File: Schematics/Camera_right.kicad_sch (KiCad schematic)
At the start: 8 parts, among them J4 Runcam Split 4 v2, U3 TPS22917DBVR

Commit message: assigned footprints ready for pcb design
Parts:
- C24, C25, C26, C27, J4: footprint (none) -> Capacitor_SMD:C_0805_2012Metric_Pad1.18x1.45mm_HandSolder
- R7, R8: footprint (none) -> Resistor_SMD:R_0805_2012Metric_Pad1.20x1.40mm_HandSolder
- U3: footprint SOT95P280X145-6N -> myFootprints:SOT95P280X145-6N
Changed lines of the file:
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@@
 			)
 		)
-		(property "Footprint" ""
+		(property "Footprint" "Capacitor_SMD:C_0805_2012Metric_Pad1.18x1.45mm_HandSolder"
 			(at 65.7352 74.93 0)
 			(effects
@@
 			)
 		)
-		(property "Footprint" ""
+		(property "Footprint" "Capacitor_SMD:C_0805_2012Metric_Pad1.18x1.45mm_HandSolder"
 			(at 134.3152 82.55 0)
 			(effects
@@
 			)
 		)
-		(property "Footprint" ""
+		(property "Footprint" "Capacitor_SMD:C_0805_2012Metric_Pad1.18x1.45mm_HandSolder"
 			(at 147.0152 82.55 0)
 			(effects
@@
 			)
 		)
-		(property "Footprint" "SOT95P280X145-6N"
+		(property "Footprint" "myFootprints:SOT95P280X145-6N"
 			(at 95.25 82.55 0)
 			(effects
@@
 			)
 		)
-		(property "Footprint" ""
+		(property "Footprint" "Resistor_SMD:R_0805_2012Metric_Pad1.20x1.40mm_HandSolder"
 			(at 197.612 71.12 90)
 			(effects
@@
 			)
 		)
-		(property "Footprint" ""
+		(property "Footprint" "Resistor_SMD:R_0805_2012Metric_Pad1.20x1.40mm_HandSolder"
 			(at 62.992 83.82 90)
 			(effects
@@
 			)
 		)
-		(property "Footprint" ""
+		(property "Footprint" "Capacitor_SMD:C_0805_2012Metric_Pad1.18x1.45mm_HandSolder"
 			(at 223.52 78.74 0)
 			(effects
@@
 			)
 		)
-		(property "Footprint" ""
+		(property "Footprint" "Capacitor_SMD:C_0805_2012Metric_Pad1.18x1.45mm_HandSolder"
 			(at 120.3452 82.55 0)
 			(effects

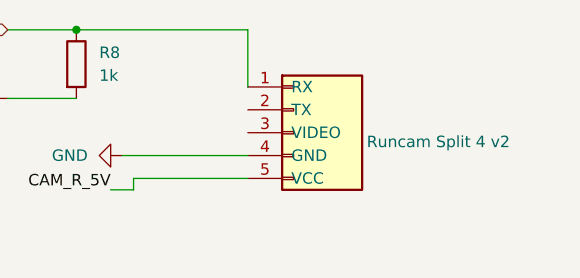
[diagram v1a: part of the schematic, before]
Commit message: Fixed Schematic and PCB refrences everything is connected correctly now
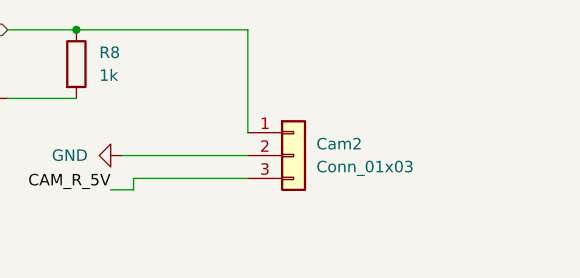
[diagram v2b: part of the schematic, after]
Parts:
- removed J4: Runcam Split 4 v2, Capacitor_SMD:C_0805_2012Metric_Pad1.18x1.45mm_HandSolder, symbol Connector_Generic:Conn_01x05
- added Cam2: Conn_01x03, Connector_JST:JST_PH_B3B-PH-K_1x03_P2.00mm_Vertical, symbol Connector_Generic:Conn_01x03
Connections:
- net CAM_UART_TX: now also Cam2.1 (Pin_1)
- net GND: now also Cam2.2 (Pin_2)
- net at C25.1, C26.1, C27.1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: now also Cam2.3 (Pin_3)
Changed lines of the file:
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@@
 	(wire
 		(pts
-			(xy 218.44 67.31) (xy 218.44 73.66)
+			(xy 218.44 67.31) (xy 218.44 78.74)
 		)
 		(stroke
@@
 	)
 	(symbol
+		(lib_id "Connector_Generic:Conn_01x03")
+		(at 223.52 81.28 0)
+		(unit 1)
+		(exclude_from_sim no)
+		(in_bom yes)
+		(on_board yes)
+		(dnp no)
+		(fields_autoplaced yes)
+		(property "Reference" "Cam2"
+			(at 226.06 80.0099 0)
+			(effects
+				(font
+					(size 1.27 1.27)
+				)
+				(justify left)
+			)
+		)
+		(property "Value" "Conn_01x03"
+			(at 226.06 82.5499 0)
+			(effects
+				(font
+					(size 1.27 1.27)
+				)
+				(justify left)
+			)
+		)
+		(property "Footprint" "Connector_JST:JST_PH_B3B-PH-K_1x03_P2.00mm_Vertical"
+			(at 223.52 81.28 0)
+			(effects
+				(font
+					(size 1.27 1.27)
+				)
+				(hide yes)
+			)
+		)
+		(property "Datasheet" "~"
+			(at 223.52 81.28 0)
+			(effects
+				(font
+					(size 1.27 1.27)
+				)
+				(hide yes)
+			)
+		)
+		(property "Description" "Generic connector, single row, 01x03, script generated (kicad-library-utils/schlib/autogen/connector/)"
+			(at 223.52 81.28 0)
+			(effects
+				(font
+					(size 1.27 1.27)
+				)
+				(hide yes)
+			)
+		)
+		(pin "1"
+		)
+		(pin "2"
+		)
+		(pin "3"
+		)
+		(instances
+			(project "CameraBoard"
+				(path "/65068a32-f105-4204-b50e-234054c5a6d0/bf3de135-4611-4c7d-8878-73765f0881dd"
+					(reference "Cam2")
+					(unit 1)
+				)
+			)
+		)
+	)
+	(symbol
 		(lib_id "power:+3.3V")
 		(at 59.69 87.63 90)
@@
 					(unit 1)
 				)
-			)
-		)
-	)
-	(symbol
-		(lib_id "Connector_Generic:Conn_01x05")
-		(at 223.52 78.74 0)
-		(unit 1)
-		(exclude_from_sim no)
-		(in_bom yes)
-		(on_board yes)
-		(dnp no)
-		(fields_autoplaced yes)
-		(property "Reference" "J4"
-			(at 226.06 77.4699 0)
-			(effects
-				(font
-					(size 1.27 1.27)
-				)
-				(justify left)
-				(hide yes)
-			)
-		)
-		(property "Value" "Runcam Split 4 v2"
-			(at 231.648 79.756 0)
-			(effects
-				(font
-					(size 1.27 1.27)
-				)
-				(justify left)
-			)
-		)
-		(property "Footprint" "Capacitor_SMD:C_0805_2012Metric_Pad1.18x1.45mm_HandSolder"
-			(at 223.52 78.74 0)
-			(effects
-				(font
-					(size 1.27 1.27)
-				)
-				(hide yes)
-			)
-		)
-		(property "Datasheet" "~"
-			(at 223.52 78.74 0)
-			(effects
-				(font
-					(size 1.27 1.27)
-				)
-				(hide yes)
-			)
-		)
-		(property "Description" "Generic connector, single row, 01x05, script generated (kicad-library-utils/schlib/autogen/connector/)"
-			(at 222.504 67.818 0)
-			(effects
-				(font
-					(size 1.27 1.27)
-				)
-				(hide yes)
-			)
-		)
-		(pin "5"
-		)
-		(pin "4"
-		)
-		(pin "3"
-		)
-		(pin "1"
-		)
-		(pin "2"
-		)
-		(instances
-			(project "cameraBoardSchematic"
-				(path "/65068a32-f105-4204-b50e-234054c5a6d0/bf3de135-4611-4c7d-8878-73765f0881dd"
-					(reference "J4")
-					(unit 1)
-				)

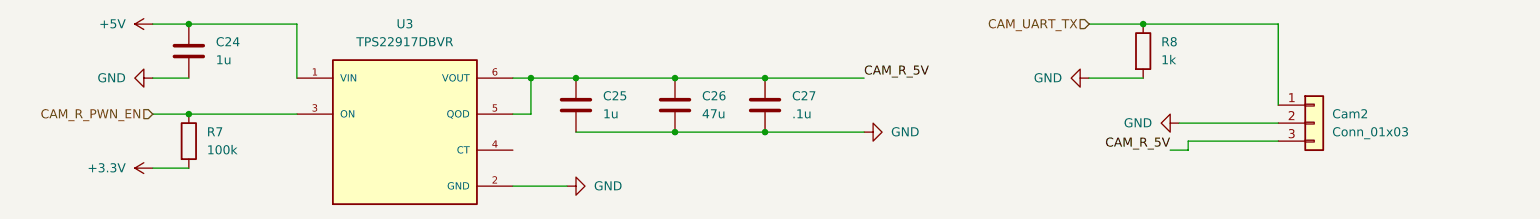
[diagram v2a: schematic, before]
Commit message: routing taking place only USB to do
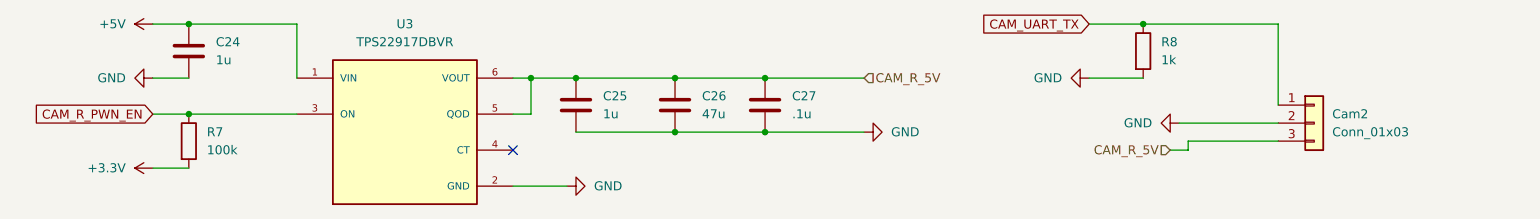
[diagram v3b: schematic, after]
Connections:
- net CAM_R_5V: now reaches C25.1, C26.1, C27.1, Cam2.3 (Pin_3), U3.5 (QOD), U3.6 (VOUT)
- no-connect marks 0 -> 1
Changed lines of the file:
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@@
 		(color 0 0 0 0)
+	)
+	(no_connect
+		(at 110.49 85.09)
 	)
 	(wire
@@
 		)
 	)
-	(label "CAM_R_5V"
-		(at 203.2 85.09 180)
+	(global_label "CAM_UART_TX"
+		(shape input)
+		(at 191.77 67.31 180)
+		(fields_autoplaced yes)
 		(effects
 			(font
 				(size 1.27 1.27)
 			)
-			(justify right bottom)
-		)
-	)
-	(label "CAM_R_5V"
-		(at 160.02 74.93 0)
-		(effects
-			(font
-				(size 1.27 1.27)
-			)
-			(justify left bottom)
-		)
-	)
-	(hierarchical_label "CAM_R_PWN_EN"
+			(justify right)
+		)
+		(property "Intersheetrefs" "${INTERSHEET_REFS}"
+			(at 176.2058 67.31 0)
+			(effects
+				(font
+					(size 1.27 1.27)
+				)
+				(justify right)
+				(hide yes)
+			)
+		)
+	)
+	(global_label "CAM_R_PWN_EN"
 		(shape input)
 		(at 59.69 80.01 180)
+		(fields_autoplaced yes)
 		(effects
 			(font
@@
 			(justify right)
 		)
-	)
-	(hierarchical_label "CAM_UART_TX"
+		(property "Intersheetrefs" "${INTERSHEET_REFS}"
+			(at 42.1906 80.01 0)
+			(effects
+				(font
+					(size 1.27 1.27)
+				)
+				(justify right)
+				(hide yes)
+			)
+		)
+	)
+	(hierarchical_label "CAM_R_5V"
 		(shape input)
-		(at 191.77 67.31 180)
-		(effects
-			(font
+		(at 160.02 74.93 0)
+		(effects
+			(font
+				(size 1.27 1.27)
+			)
+			(justify left)
+		)
+	)
+	(hierarchical_label "CAM_R_5V"
+		(shape input)
+		(at 203.2 85.09 180)
+		(effects
+			(font

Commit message: Cleaned up schematic added ocilator added jtag 10 pin begining routing again
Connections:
- net CAM_R_5V: no longer names the net of C25.1, C26.1, C27.1, Cam2.3 (Pin_3), U3.5 (QOD), U3.6 (VOUT)
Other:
- moved on the sheet: R8
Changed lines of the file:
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@@
 	)
 	(junction
-		(at 199.39 67.31)
+		(at 199.39 73.66)
 		(diameter 0)
 		(color 0 0 0 0)
@@
 		(color 0 0 0 0)
 	)
+	(junction
+		(at 199.39 81.28)
+		(diameter 0)
+		(color 0 0 0 0)
+	)
 	(no_connect
 		(at 110.49 85.09)
@@
 	(wire
 		(pts
-			(xy 191.77 67.31) (xy 199.39 67.31)
+			(xy 191.77 73.66) (xy 199.39 73.66)
 		)
 		(stroke
@@
 	(wire
 		(pts
-			(xy 204.47 81.28) (xy 218.44 81.28)
+			(xy 187.96 81.28) (xy 199.39 81.28)
+		)
+		(stroke
+			(width 0)
+			(type default)
+		)
+	)
+	(wire
+		(pts
+			(xy 199.39 81.28) (xy 218.44 81.28)
 		)
 		(stroke
@@
 	(wire
 		(pts
-			(xy 191.77 74.93) (xy 199.39 74.93)
-		)
-		(stroke
-			(width 0)
-			(type default)
-		)
-	)
-	(wire
-		(pts
 			(xy 133.35 82.55) (xy 146.05 82.55)
 		)
@@
 	(wire
 		(pts
-			(xy 203.2 85.09) (xy 205.74 85.09)
+			(xy 187.96 85.09) (xy 205.74 85.09)
 		)
 		(stroke
@@
 	(wire
 		(pts
-			(xy 199.39 67.31) (xy 218.44 67.31)
+			(xy 199.39 73.66) (xy 218.44 73.66)
 		)
 		(stroke
@@
 	(wire
 		(pts
-			(xy 218.44 67.31) (xy 218.44 78.74)
+			(xy 218.44 73.66) (xy 218.44 78.74)
 		)
 		(stroke
@@
 		)
 	)
-	(global_label "CAM_UART_TX"
-		(shape input)
-		(at 191.77 67.31 180)
-		(fields_autoplaced yes)
-		(effects
-			(font
-				(size 1.27 1.27)
-			)
-			(justify right)
-		)
-		(property "Intersheetrefs" "${INTERSHEET_REFS}"
-			(at 176.2058 67.31 0)
-			(effects
-				(font
-					(size 1.27 1.27)
-				)
-				(justify right)
-				(hide yes)
-			)
-		)
-	)
-	(global_label "CAM_R_PWN_EN"
-		(shape input)
-		(at 59.69 80.01 180)
-		(fields_autoplaced yes)
-		(effects
-			(font
-				(size 1.27 1.27)
-			)
-			(justify right)
-		)
-		(property "Intersheetrefs" "${INTERSHEET_REFS}"
-			(at 42.1906 80.01 0)
-			(effects
-				(font
-					(size 1.27 1.27)
-				)
-				(justify right)
-				(hide yes)
-			)
-		)
-	)
-	(hierarchical_label "CAM_R_5V"
-		(shape input)
+	(label "CAM_R_5V"
 		(at 160.02 74.93 0)
 		(effects
@@
 				(size 1.27 1.27)
 			)
-			(justify left)
-		)
-	)
-	(hierarchical_label "CAM_R_5V"
+			(justify left bottom)
+		)
+	)
+	(label "CAM_R_5V"
+		(at 187.96 85.09 180)
+		(effects
+			(font
+				(size 1.27 1.27)
+			)
+			(justify right bottom)
+		)
+	)
+	(hierarchical_label "CAM_UART_TX"
 		(shape input)
-		(at 203.2 85.09 180)
+		(at 191.77 73.66 180)
+		(effects
+			(font
+				(size 1.27 1.27)
+			)
+			(justify right)
+		)
+	)
+	(hierarchical_label "CAM_R_PWN_EN"
+		(shape input)
+		(at 59.69 80.01 180)
 		(effects
 			(font
@@
 	)
 	(symbol
-		(lib_id "power:GND")
-		(at 191.77 74.93 270)
-		(unit 1)
-		(exclude_from_sim no)
-		(in_bom yes)
-		(on_board yes)
-		(dnp no)
-		(fields_autoplaced yes)
-		(property "Reference" "#PWR033"
-			(at 185.42 74.93 0)
-			(effects
-				(font
-					(size 1.27 1.27)
-				)
-				(hide yes)
-			)
-		)
-		(property "Value" "GND"
-			(at 187.96 74.9299 90)
-			(effects
-				(font
-					(size 1.27 1.27)
-				)
-				(justify right)
-			)
-		)
-		(property "Footprint" ""
-			(at 191.77 74.93 0)
-			(effects
-				(font
-					(size 1.27 1.27)
-				)
-				(hide yes)
-			)
-		)
-		(property "Datasheet" ""
-			(at 191.77 74.93 0)
-			(effects
-				(font
-					(size 1.27 1.27)
-				)
-				(hide yes)
-			)
-		)
-		(property "Description" "Power symbol creates a global label with name \"GND\" , ground"
-			(at 191.77 74.93 0)
-			(effects
-				(font
-					(size 1.27 1.27)
-				)
-				(hide yes)
-			)
-		)
-		(pin "1"
-		)
-		(instances
-			(project "cameraBoardSchematic"
-				(path "/65068a32-f105-4204-b50e-234054c5a6d0/bf3de135-4611-4c7d-8878-73765f0881dd"
-					(reference "#PWR033")
-					(unit 1)
-				)
-			)
-		)
-	)
-	(symbol
 		(lib_id "Connector_Generic:Conn_01x03")
 		(at 223.52 81.28 0)
@@
 	(symbol
 		(lib_id "Device:R")
-		(at 199.39 71.12 0)
+		(at 199.39 77.47 0)
 		(unit 1)
 		(exclude_from_sim no)
@@
 		(fields_autoplaced yes)
 		(property "Reference" "R8"
-			(at 201.93 69.8499 0)
+			(at 201.93 76.1999 0)
 			(effects
 				(font
@@
 		)
 		(property "Value" "1k"
-			(at 201.93 72.3899 0)
+			(at 201.93 78.7399 0)
 			(effects
 				(font
@@
 		)
 		(property "Footprint" "Resistor_SMD:R_0805_2012Metric_Pad1.20x1.40mm_HandSolder"
-			(at 197.612 71.12 90)
+			(at 197.612 77.47 90)
 			(effects
 				(font
@@
 		)
 		(property "Datasheet" "~"
-			(at 199.39 71.12 0)
+			(at 199.39 77.47 0)
 			(effects
 				(font
@@
 		)
 		(property "Description" "Resistor"
-			(at 199.39 71.12 0)
+			(at 199.39 77.47 0)
 			(effects
 				(font
@@
 	(symbol
 		(lib_id "power:GND")
-		(at 204.47 81.28 270)
+		(at 187.96 81.28 270)
 		(unit 1)
 		(exclude_from_sim no)
@@
 		(fields_autoplaced yes)
 		(property "Reference" "#PWR034"
-			(at 198.12 81.28 0)
+			(at 181.61 81.28 0)
 			(effects
 				(font
@@
 		)
 		(property "Value" "GND"
-			(at 200.66 81.2799 90)
+			(at 184.15 81.2799 90)
 			(effects
 				(font
@@
 		)
 		(property "Footprint" ""
-			(at 204.47 81.28 0)
+			(at 187.96 81.28 0)
 			(effects
 				(font
@@
 		)
 		(property "Datasheet" ""
-			(at 204.47 81.28 0)
+			(at 187.96 81.28 0)
 			(effects
 				(font
@@
 		)
 		(property "Description" "Power symbol creates a global label with name \"GND\" , ground"
-			(at 204.47 81.28 0)
-			(effects
-				(font
+			(at 187.96 81.28 0)
+			(effects
+				(font

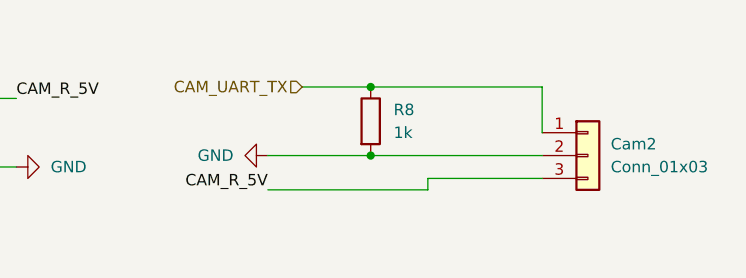
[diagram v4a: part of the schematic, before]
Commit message: second final draft finished routing added swd debug with stlink capabilities pending review for and data sheet review to ensure parts are correct, also need to edge cut ocillator
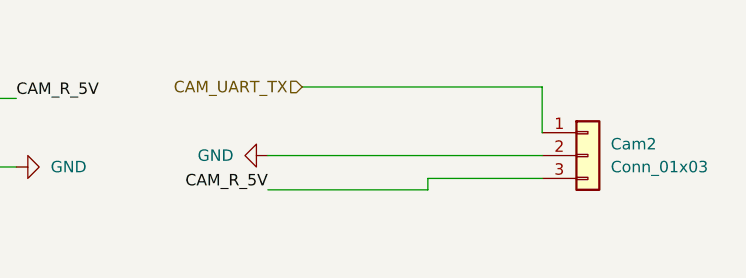
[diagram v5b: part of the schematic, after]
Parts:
- removed R8: 1k, Resistor_SMD:R_0805_2012Metric_Pad1.20x1.40mm_HandSolder, symbol Device:R
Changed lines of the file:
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@@
-	)
-	(junction
-		(at 199.39 73.66)
-		(diameter 0)
-		(color 0 0 0 0)
 	)
 	(junction
@@
 		(color 0 0 0 0)
 	)
-	(junction
-		(at 199.39 81.28)
-		(diameter 0)
-		(color 0 0 0 0)
-	)
 	(no_connect
 		(at 110.49 85.09)
@@
 	(wire
 		(pts
-			(xy 191.77 73.66) (xy 199.39 73.66)
+			(xy 191.77 73.66) (xy 218.44 73.66)
 		)
 		(stroke
@@
 	(wire
 		(pts
-			(xy 187.96 81.28) (xy 199.39 81.28)
-		)
-		(stroke
-			(width 0)
-			(type default)
-		)
-	)
-	(wire
-		(pts
-			(xy 199.39 81.28) (xy 218.44 81.28)
+			(xy 187.96 81.28) (xy 218.44 81.28)
 		)
 		(stroke
@@
 		(pts
 			(xy 59.69 67.31) (xy 64.77 67.31)
-		)
-		(stroke
-			(width 0)
-			(type default)
-		)
-	)
-	(wire
-		(pts
-			(xy 199.39 73.66) (xy 218.44 73.66)
 		)
 		(stroke
@@
 					(unit 1)
 				)
-			)
-		)
-	)
-	(symbol
-		(lib_id "Device:R")
-		(at 199.39 77.47 0)
-		(unit 1)
-		(exclude_from_sim no)
-		(in_bom yes)
-		(on_board yes)
-		(dnp no)
-		(fields_autoplaced yes)
-		(property "Reference" "R8"
-			(at 201.93 76.1999 0)
-			(effects
-				(font
-					(size 1.27 1.27)
-				)
-				(justify left)
-			)
-		)
-		(property "Value" "1k"
-			(at 201.93 78.7399 0)
-			(effects
-				(font
-					(size 1.27 1.27)
-				)
-				(justify left)
-			)
-		)
-		(property "Footprint" "Resistor_SMD:R_0805_2012Metric_Pad1.20x1.40mm_HandSolder"
-			(at 197.612 77.47 90)
-			(effects
-				(font
-					(size 1.27 1.27)
-				)
-				(hide yes)
-			)
-		)
-		(property "Datasheet" "~"
-			(at 199.39 77.47 0)
-			(effects
-				(font
-					(size 1.27 1.27)
-				)
-				(hide yes)
-			)
-		)
-		(property "Description" "Resistor"
-			(at 199.39 77.47 0)
-			(effects
-				(font
-					(size 1.27 1.27)
-				)
-				(hide yes)
-			)
-		)
-		(pin "2"
-		)
-		(pin "1"
-		)
-		(instances
-			(project "cameraBoardSchematic"
-				(path "/65068a32-f105-4204-b50e-234054c5a6d0/bf3de135-4611-4c7d-8878-73765f0881dd"
-					(reference "R8")
-					(unit 1)
-				)
